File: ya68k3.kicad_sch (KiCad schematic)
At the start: 10 parts, among them SW1 SW_Push, U1 MC68008P, U2 74HC05, U3 MAX708, U4 XTAL_OSC_HALF_CAN

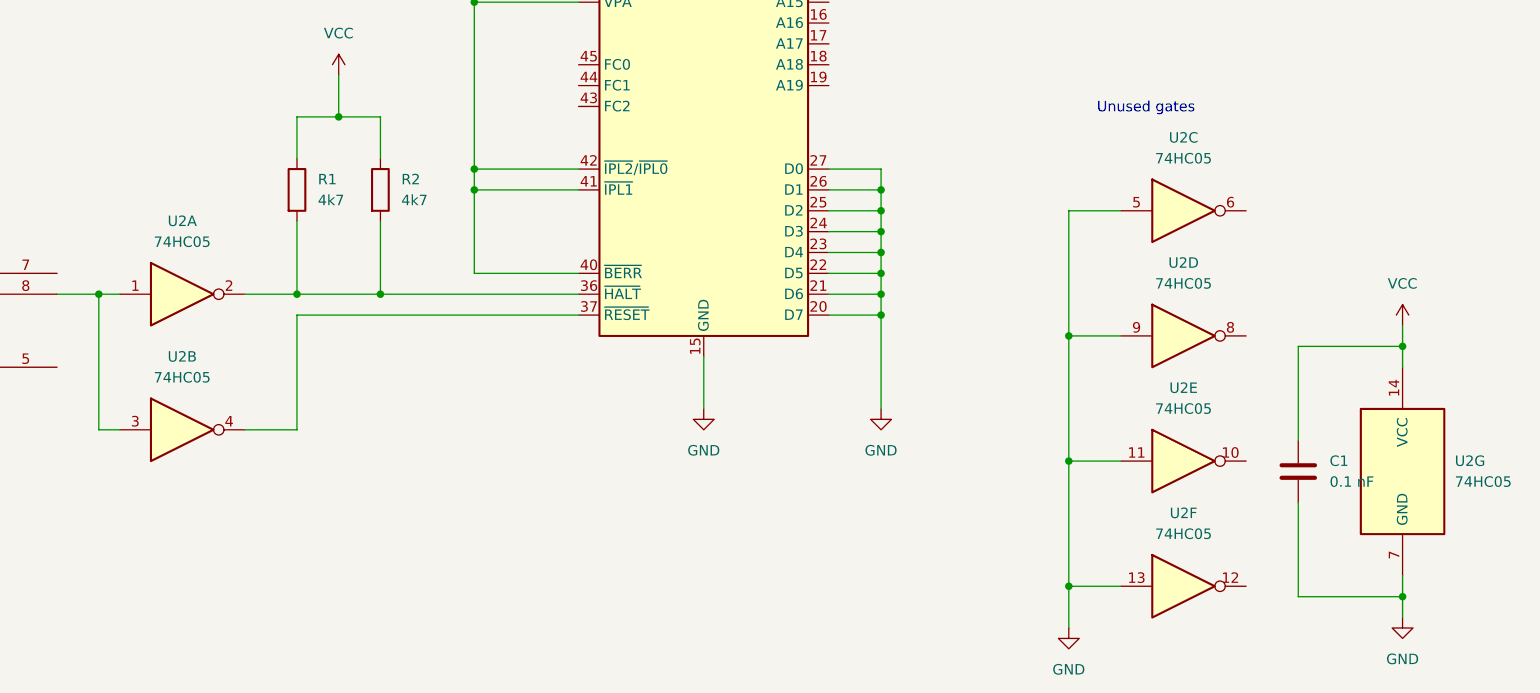
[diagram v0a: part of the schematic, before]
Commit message: change 74HC05 to 74LS05
I don't think the MAX708 has a high enough output high voltage
to be guaranteed to drive an input of a 74HC chip - it's listed
as Vcc-1.5, which could be less than 70% of Vcc.
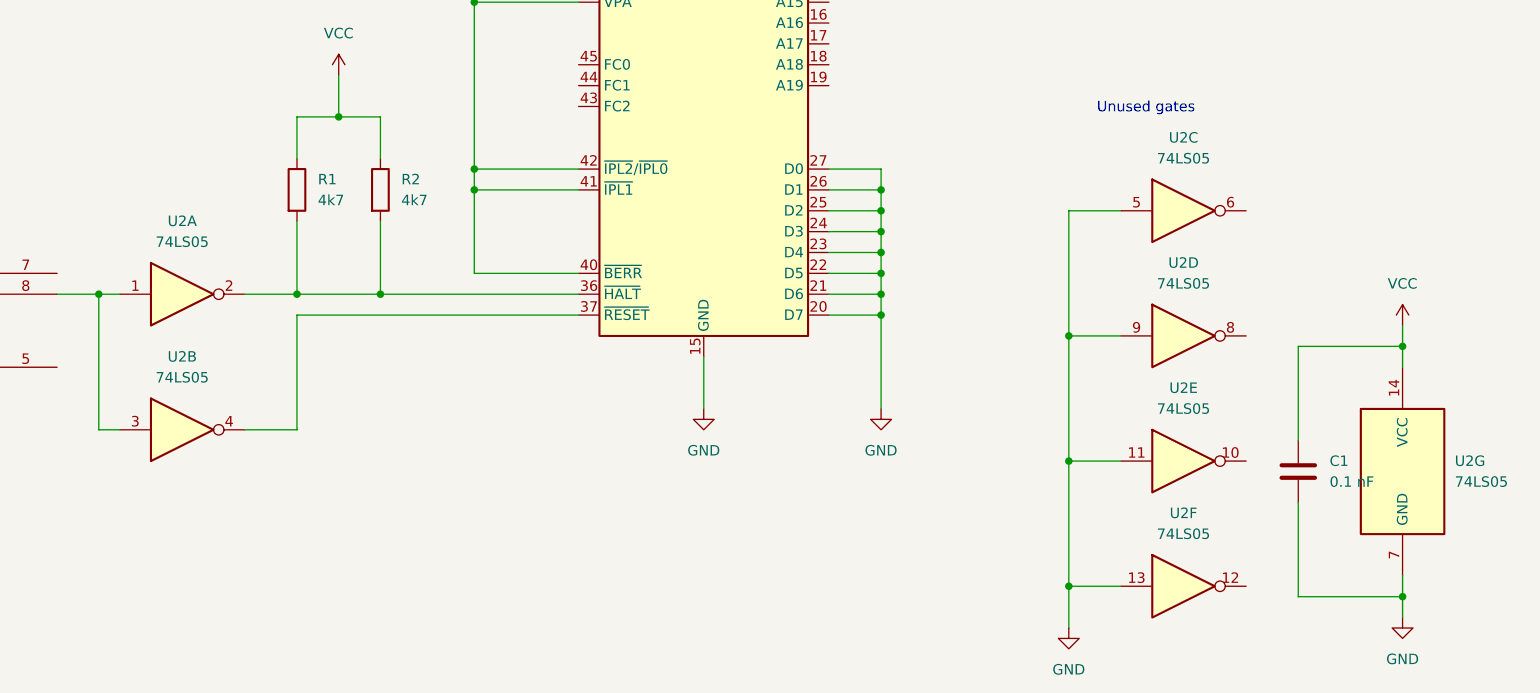
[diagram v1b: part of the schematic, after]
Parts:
- U2: value 74HC05 -> 74LS05
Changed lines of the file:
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@@
 			)
 		)
-		(property "Value" "74HC05"
+		(property "Value" "74LS05"
 			(at 220.98 97.79 0)
 			(effects
@@
 			)
 		)
-		(property "Value" "74HC05"
+		(property "Value" "74LS05"
 			(at 220.98 128.27 0)
 			(effects
@@
 			)
 		)
-		(property "Value" "74HC05"
+		(property "Value" "74LS05"
 			(at 220.98 143.51 0)
 			(effects
@@
 			)
 		)
-		(property "Value" "74HC05"
+		(property "Value" "74LS05"
 			(at 99.06 107.95 0)
 			(effects
@@
 			)
 		)
-		(property "Value" "74HC05"
+		(property "Value" "74LS05"
 			(at 99.06 124.46 0)
 			(effects
@@
 			)
 		)
-		(property "Value" "74HC05"
+		(property "Value" "74LS05"
 			(at 254 137.1599 0)
 			(effects
@@
 			)
 		)
-		(property "Value" "74HC05"
+		(property "Value" "74LS05"
 			(at 220.98 113.03 0)
 			(effects
